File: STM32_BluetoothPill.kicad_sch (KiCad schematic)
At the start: 1 part, among them U1 STM32WBxx

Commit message: Power supply and GPIO
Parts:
- added C? (x2): 4.7u, symbol Device:C_Small
- added C? (x9): 100n, symbol Device:C_Small
- added C? (x2): 12p, symbol Device:C_Small
- added C? (x2): 1u, symbol Device:C_Small
- added C? (x2): 10p, symbol Device:C_Small
- added C?: 10n, symbol Device:C_Small
- added C?: 100p, symbol Device:C_Small
- added D?: GRN, symbol Device:LED_Small
- added D?: PWR, symbol Device:LED_Small
- added D?: RED, symbol Device:LED_Small
- added D?: BLU, symbol Device:LED_Small
- added J?: USB_C_Receptacle_USB2.0, symbol Connector:USB_C_Receptacle_USB2.0
- added J? (x2): Conn_01x20, symbol Connector_Generic:Conn_01x20
- added J?: Conn_01x05, symbol Connector_Generic:Conn_01x05
- added JP?: Jumper_3_Open, symbol Jumper:Jumper_3_Open
- added L?: L_Small, symbol Device:L_Small
- added R?: NC, symbol Device:R_Small
- added R? (x4): 680, symbol Device:R_Small
- added R?: 1k, symbol Device:R_Small
- added R?: 10k, symbol Device:R_Small
- added R? (x2): 5.1k, symbol Device:R_Small
- added R?: 0, symbol Device:R_Small
- added SW?: Reset, symbol Switch:SW_Push
- added SW?: User PB, symbol Switch:SW_Push
- added U?: USBLC6-2SC6, Package_TO_SOT_SMD:SOT-23-6, symbol Power_Protection:USBLC6-2SC6
- added U?: LD3985M33R_SOT23, Package_TO_SOT_SMD:SOT-23-5, symbol Regulator_Linear:LD3985M33R_SOT23
- added Y?: 32k768, symbol Device:Crystal_Small
- added Y?: 8M, symbol Device:Crystal_Small
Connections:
- net VBAT: now reaches U1.1 (VBAT)
- net VBAT: now also J?.20 (Pin_20)
- net PA1: now reaches U1.10 (PA1)
- net PA1: now also J?.16 (Pin_16)
- net PA2: now reaches U1.11 (PA2)
- net PA2: now also J?.15 (Pin_15)
- net PA3: now reaches U1.12 (PA3)
- net PA3: now also J?.14 (Pin_14)
- net PA4: now reaches U1.13 (PA4)
- net PA4: now also J?.13 (Pin_13)
- net PA5: now reaches U1.14 (PA5)
- net PA5: now also J?.12 (Pin_12)
- net PA6: now reaches U1.15 (PA6)
- net PA6: now also J?.11 (Pin_11)
- net PA7: now reaches U1.16 (PA7)
- net PA7: now also J?.10 (Pin_10)
- net PA8: now reaches U1.17 (PA8)
- net PA8: now also J?.9 (Pin_9)
- net PA9: now reaches U1.18 (PA9)
- net PA9: now also J?.8 (Pin_8)
- net PB2: now reaches U1.19 (PB2)
- net PB2: now also J?.7 (Pin_7)
- net at U1.2 (PC14-OSC32_IN): now also C?.1, Y?.2
- net +3V3: now reaches U1.20 (VDD), U1.35 (VDD), U1.48 (VDD)
- net +3V3: now also U1.23 (VDDRF), U1.34 (VDDSMPS), U1.40 (VDDUSB), U1.8 (VDDA), C?.1, C?.1, C?.1, C?.1, C?.1, C?.1, C?.2, C?.2, J?.1 (Pin_1), J?.20 (Pin_20), J?.3 (Pin_3), JP?.1 (A), R?.1, R?.1, R?.1, R?.2
- net GND: now reaches U1.22 (VSSRF)
- net GND: now also U1.32 (VSSSMPS), U1.49 (EXP), C?.1, C?.1, C?.1, C?.2, C?.2, C?.2, C?.2, C?.2, C?.2, C?.2, C?.2, C?.2, C?.2, C?.2, C?.2, C?.2, C?.2, C?.2, C?.2, D?.1 (K), D?.1 (K), D?.1 (K), D?.1 (K), J?.1 (Pin_1), J?.19 (Pin_19), J?.2 (Pin_2), J?.4 (Pin_4), J?.A1 (GND), J?.A12 (GND), J?.B1 (GND), J?.B12 (GND), J?.S1 (SHIELD), JP?.3 (B), R?.1, R?.2, SW?.1, SW?.1, U?.2 (GND), U?.2 (GND)
- net at U1.24 (OSC_OUT): now also C?.1, Y?.2
- net at U1.25 (OSC_IN): now also C?.1, Y?.1
- net PB0: now reaches U1.28 (PB0)
- net PB0: now also J?.6 (Pin_6), R?.1
- net PB1: now reaches U1.29 (PB1)
- net PB1: now also J?.7 (Pin_7), R?.1
- net at U1.3 (PC15-OSC32_OUT): now also C?.1, Y?.1
- net PE4: now reaches U1.30 (PE4)
- net PE4: now also J?.8 (Pin_8), R?.1
- net at U1.31 (VFBSMPS): now also C?.2, L?.2, R?.1
- net at U1.33 (VLXSMPS): now also L?.1
- net PA10: now reaches U1.36 (PA10)
- net PA10: now also J?.9 (Pin_9), R?.1
- net USB_N: now reaches U1.37 (PA11)
- net USB_N: now also J?.10 (Pin_10), U?.6 (I/O1)
- net USB_P: now reaches U1.38 (PA12)
- net USB_P: now also J?.11 (Pin_11), U?.4 (I/O2)
- net SWDIO: now reaches U1.39 (PA13)
- net SWDIO: now also J?.2 (Pin_2)
- net at U1.4 (PH3-BOOT0): now also JP?.2 (C)
- net SWCLK: now reaches U1.41 (PA14)
- net SWCLK: now also J?.3 (Pin_3)
- net PA15: now reaches U1.42 (PA15)
- net PA15: now also J?.12 (Pin_12)
- net PB3: now reaches U1.43 (PB3)
- net PB3: now also J?.13 (Pin_13), J?.5 (Pin_5)
- net PB4: now reaches U1.44 (PB4)
- net PB4: now also J?.14 (Pin_14)
- net PB5: now reaches U1.45 (PB5)
- net PB5: now also J?.15 (Pin_15)
- net PB6: now reaches U1.46 (PB6)
- net PB6: now also J?.16 (Pin_16)
- net PB7: now reaches U1.47 (PB7)
- net PB7: now also J?.17 (Pin_17)
- net PB8: now reaches U1.5 (PB8)
- net PB8: now also J?.19 (Pin_19)
- net PB9: now reaches U1.6 (PB9)
- net PB9: now also J?.18 (Pin_18)
- net RESET: now reaches U1.7 (NRST)
- net RESET: now also C?.1, J?.4 (Pin_4), R?.2, SW?.2
- net PA0: now reaches U1.9 (PA0)
- net PA0: now also J?.17 (Pin_17)
- new net: D?.2 (A), R?.2 (x4)
- new net: J?.A5 (CC1), R?.2
- new net: J?.A6 (D+), J?.B6 (D+), U?.3 (I/O2)
- new net: J?.A7 (D-), J?.B7 (D-), U?.1 (I/O1)
- new net: J?.B5 (CC2), R?.1
- new net: C?.1, C?.1, R?.2, U?.5 (VOUT)
- new net: R?.2, SW?.2
- new net: C?.1, U?.4 (BYP)
- new net +5V: C?.1, C?.1, J?.18 (Pin_18), J?.A4 (VBUS), J?.A9 (VBUS), J?.B4 (VBUS), J?.B9 (VBUS), U?.1 (VIN), U?.3 (INH), U?.5 (VBUS)
- no-connect marks 0 -> 4

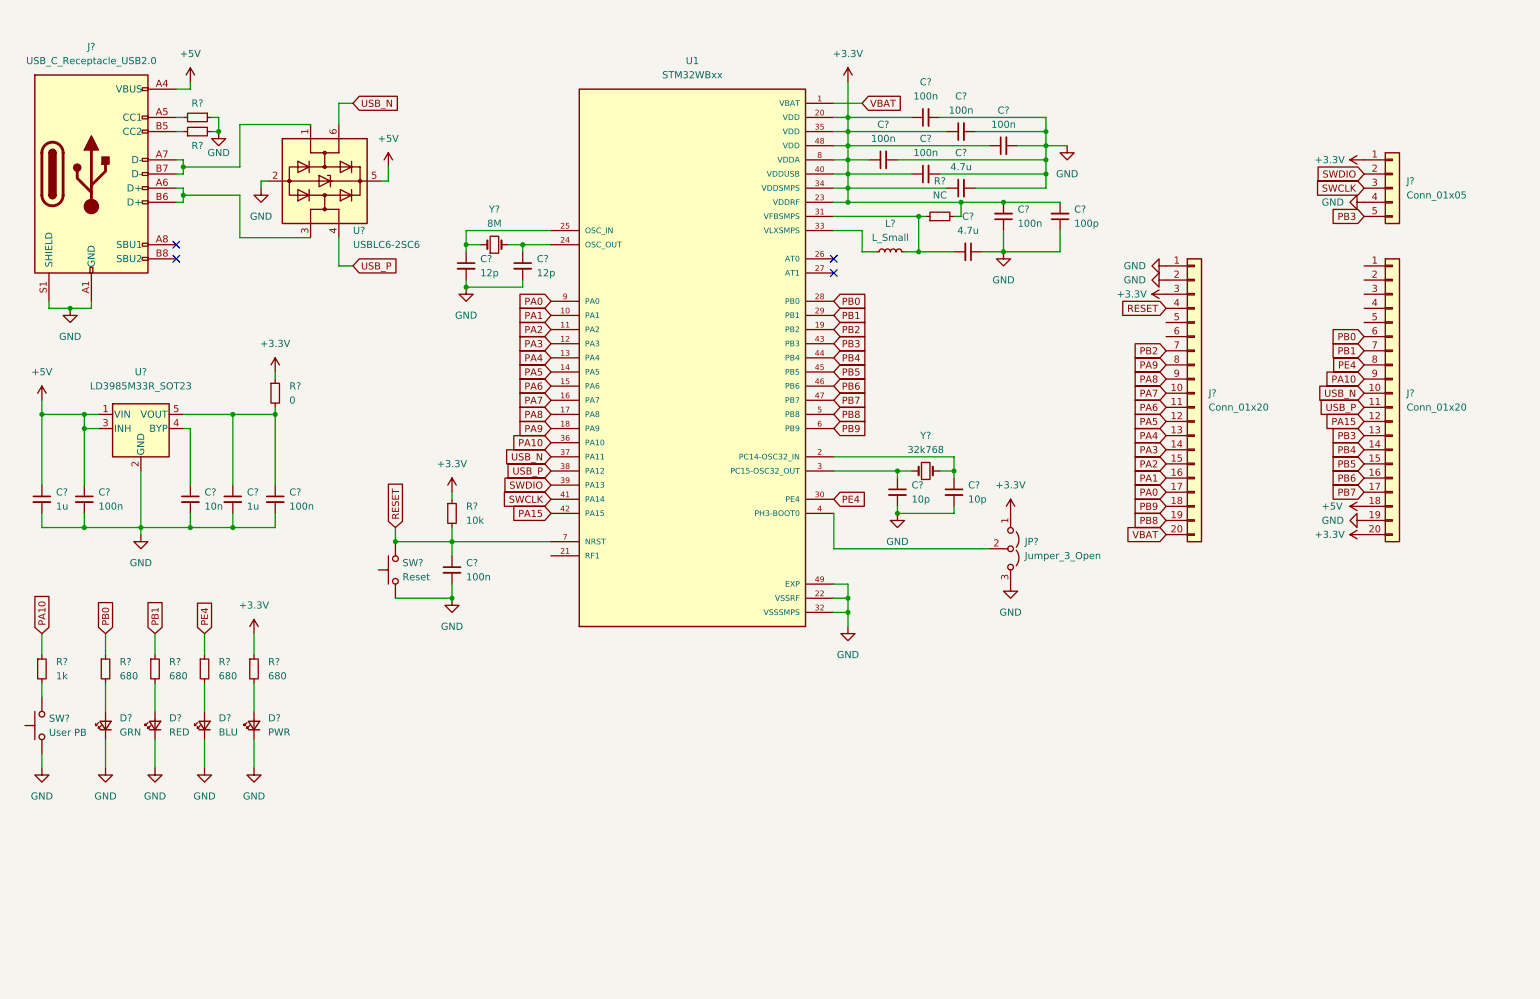
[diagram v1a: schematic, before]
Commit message: RF shield
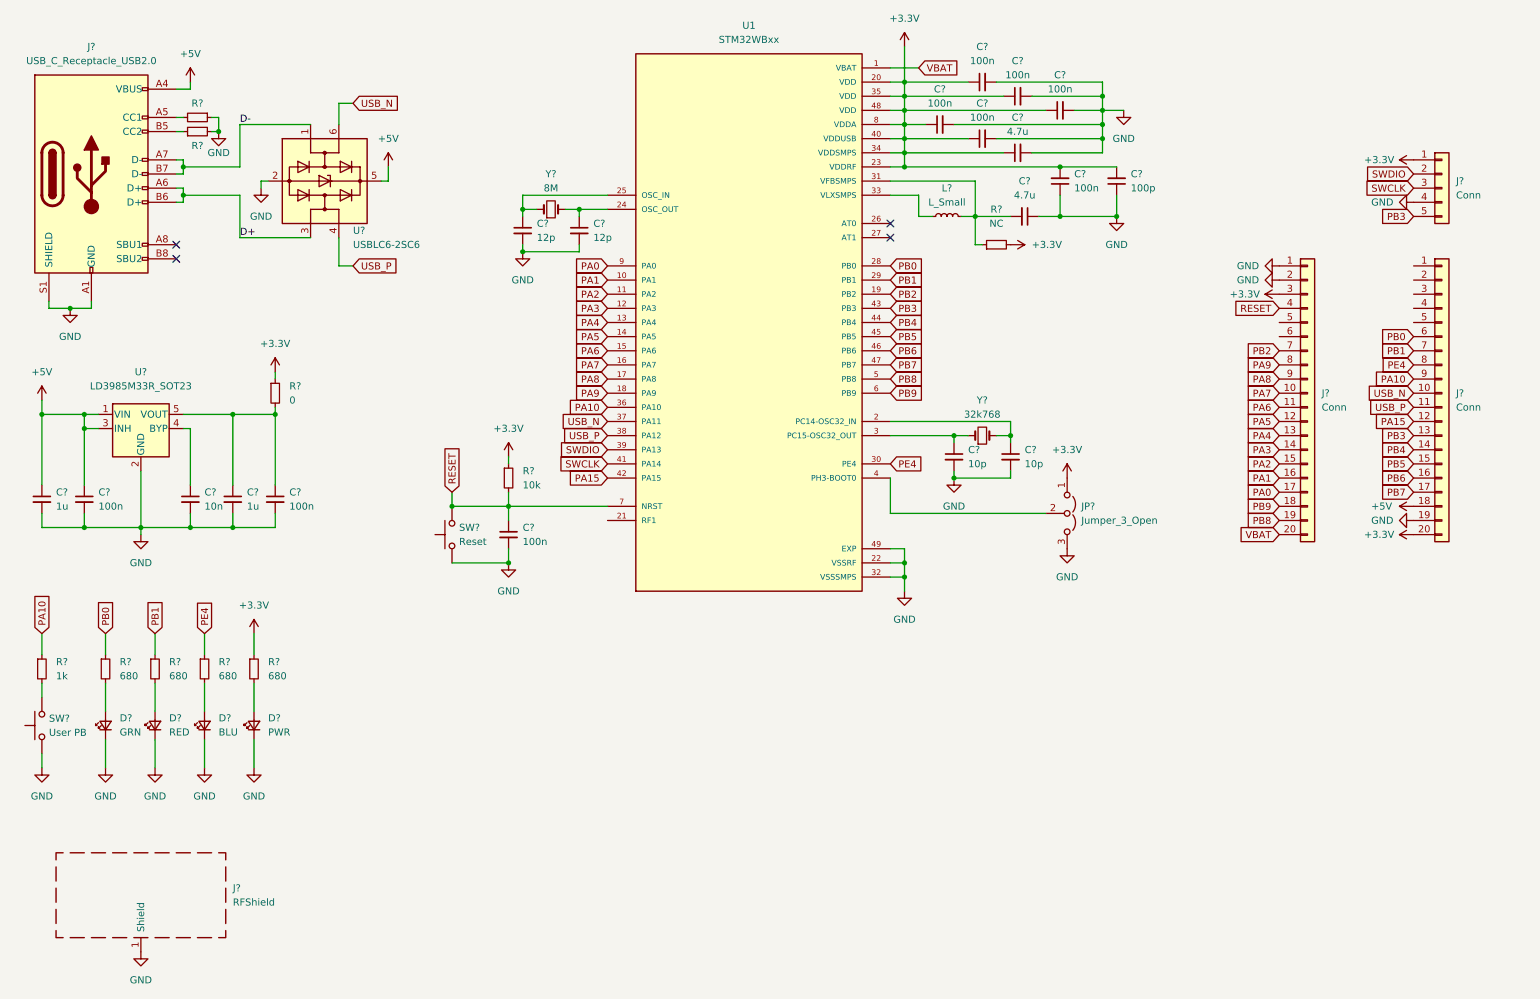
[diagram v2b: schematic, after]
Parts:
- added J?: RFShield, symbol Device:RFShield_OnePiece
- J? (x2): value Conn_01x20 -> Conn
- J?: value Conn_01x05 -> Conn
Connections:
- net GND: now also J?.1 (Shield)
- net D+: now reaches J?.A6 (D+), J?.B6 (D+), U?.3 (I/O2)
- net D-: now reaches J?.A7 (D-), J?.B7 (D-), U?.1 (I/O1)
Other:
- moved on the sheet: C?, J?, JP?, L?, R?, SW?, U1, Y?

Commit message: footprints designated
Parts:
- removed J?: USB_C_Receptacle_USB2.0, symbol Connector:USB_C_Receptacle_USB2.0
- removed J? (x2): Conn, symbol Connector_Generic:Conn_01x20
- removed J?: Conn, symbol Connector_Generic:Conn_01x05
- removed R? (x2): 5.1k, symbol Device:R_Small
- added J1: USB_A, lib:CONN-USB-A-PCB-TRACES, symbol Connector:USB_A
- added J2: Conn, Connector_PinHeader_2.54mm:PinHeader_1x04_P2.54mm_Vertical, symbol Connector_Generic:Conn_01x04
- added J3, J4: Conn, Connector_PinHeader_2.54mm:PinHeader_1x16_P2.54mm_Vertical, symbol Connector_Generic:Conn_01x16
- C1, C10, C11, C12, C13, C14, C15, C16, C17, C18, C19, C2, C3, C4, C5, C6, C7, C8, C9: renamed from C?; footprint (none) -> Capacitor_SMD:C_0603_1608Metric_Pad1.08x0.95mm_HandSolder
- D1, D2, D3, D4: renamed from D?; footprint (none) -> Capacitor_SMD:C_0603_1608Metric_Pad1.08x0.95mm_HandSolder
- J5: renamed from J?; footprint (none) -> RF_Shielding:Laird_Technologies_BMI-S-202-F_16.50x16.50mm
- JP1: renamed from JP?; footprint (none) -> Connector_PinHeader_2.54mm:PinHeader_1x03_P2.54mm_Vertical
- L1: renamed from L?; value L_Small -> 10u; footprint (none) -> Inductor_SMD:L_1206_3216Metric_Pad1.42x1.75mm_HandSolder
- R10, R3, R4, R5, R6, R7, R8, R9: renamed from R?; footprint (none) -> Resistor_SMD:R_0603_1608Metric_Pad0.98x0.95mm_HandSolder
- SW1, SW2: renamed from SW?; footprint (none) -> Button_Switch_SMD:SW_SPST_CK_RS282G05A3
- U1: footprint lib:QFN50P700X700X60-49N -> Package_DFN_QFN:QFN-48-1EP_7x7mm_P0.5mm_EP5.6x5.6mm
- Y1: renamed from Y?; footprint (none) -> Crystal:Crystal_HC49-4H_Vertical
- Y2: renamed from Y?; footprint (none) -> Crystal:Crystal_SMD_SeikoEpson_MC306-4Pin_8.0x3.2mm
- gave numbers to parts that had none: 2
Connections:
- net +3V3: now also J2.1 (Pin_1), J3.2 (Pin_2), J4.16 (Pin_16)
- net +5V: now also J1.1 (VBUS), J4.14 (Pin_14)
- net D+: now also J1.2 (D-)
- net D-: now also J1.3 (D+)
- net GND: now also J1.4 (GND), J2.4 (Pin_4), J3.1 (Pin_1), J4.1 (Pin_1), J4.15 (Pin_15)
- net PA0: now also J3.14 (Pin_14)
- net PA1: now also J3.13 (Pin_13)
- net PA10: now also J4.5 (Pin_5)
- net PA15: now also J4.8 (Pin_8)
- net PA2: now also J3.12 (Pin_12)
- net PA3: now also J3.11 (Pin_11)
- net PA4: now also J3.10 (Pin_10)
- net PA5: now also J3.9 (Pin_9)
- net PA6: now also J3.8 (Pin_8)
- net PA7: now also J3.7 (Pin_7)
- net PA8: now also J3.6 (Pin_6)
- net PA9: now also J3.5 (Pin_5)
- net PB0: now also J4.2 (Pin_2)
- net PB1: now also J4.3 (Pin_3)
- net PB2: now also J3.4 (Pin_4)
- net PB3: now also J4.9 (Pin_9)
- net PB4: now also J4.10 (Pin_10)
- net PB5: now also J4.11 (Pin_11)
- net PB6: now also J4.12 (Pin_12)
- net PB7: now also J4.13 (Pin_13)
- net PB8: now also J3.16 (Pin_16)
- net PB9: now also J3.15 (Pin_15)
- net PE4: now also J4.4 (Pin_4)
- net RESET: now also J3.3 (Pin_3)
- net SWCLK: now also J2.3 (Pin_3)
- net SWDIO: now also J2.2 (Pin_2)
- net USB_N: now also J4.6 (Pin_6)
- net USB_P: now also J4.7 (Pin_7)
- net VBAT: no longer names the net of U1.1 (VBAT)
- no-connect marks 4 -> 3

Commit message: footprints changed gpio names added
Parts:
- C1, C10, C11, C12, C13, C14, C15, C16, C17, C18, C19, C2, C3, C4, C5, C6, C7, C8, C9, D1, D2, D3, D4: footprint Capacitor_SMD:C_0603_1608Metric_Pad1.08x0.95mm_HandSolder -> Capacitor_SMD:C_0603_1608Metric
- R10, R3, R4, R5, R6, R7, R8, R9: footprint Resistor_SMD:R_0603_1608Metric_Pad0.98x0.95mm_HandSolder -> Resistor_SMD:R_0603_1608Metric
- Y1: footprint Crystal:Crystal_HC49-4H_Vertical -> Crystal:Crystal_SMD_HC49-SD
- Y2: footprint Crystal:Crystal_SMD_SeikoEpson_MC306-4Pin_8.0x3.2mm -> Crystal:Crystal_SMD_G8-2Pin_3.2x1.5mm

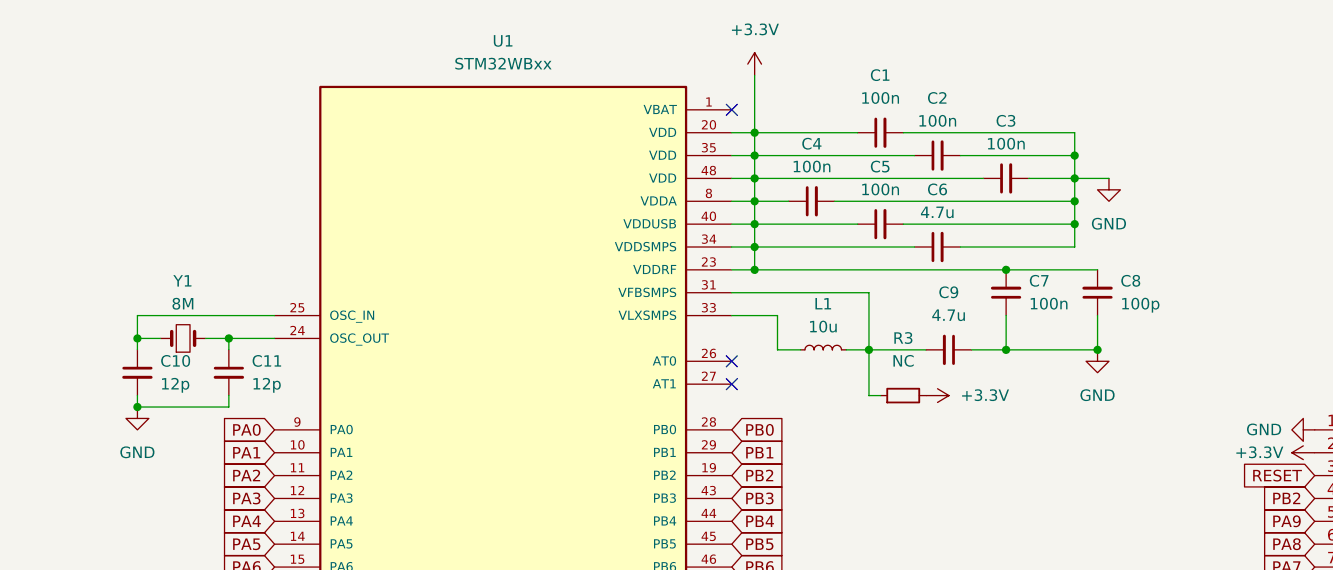
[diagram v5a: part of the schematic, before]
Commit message: move to kicad 6 footprint updates
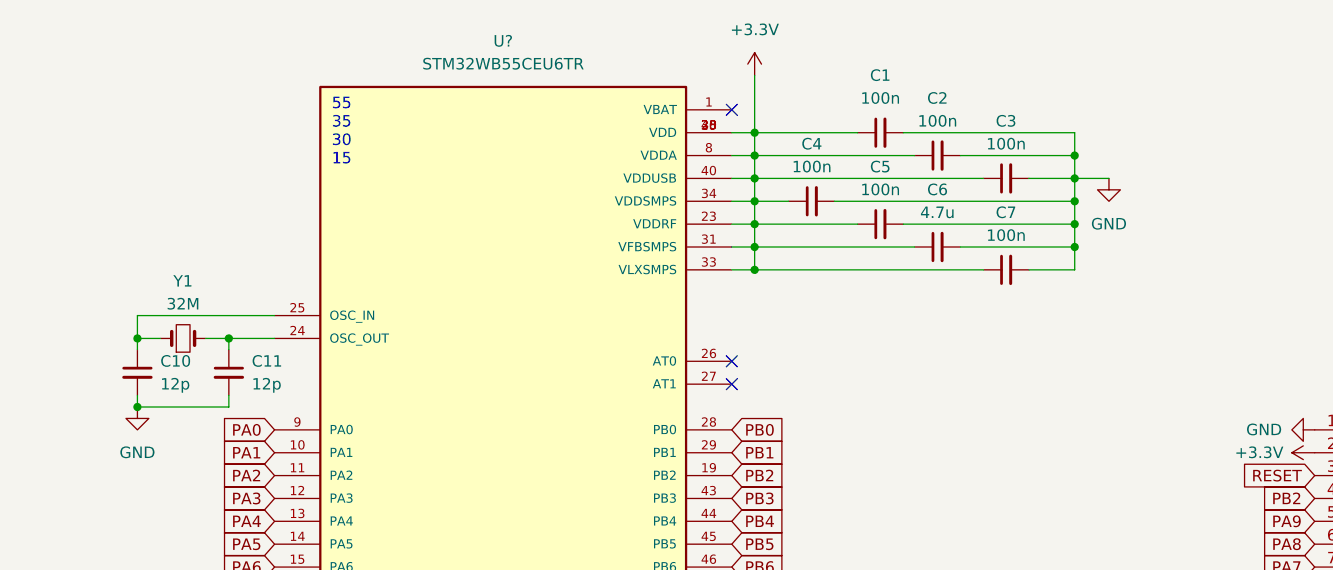
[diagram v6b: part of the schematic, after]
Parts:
- removed C8: 100p, Capacitor_SMD:C_0603_1608Metric, symbol Device:C_Small
- removed C9: 4.7u, Capacitor_SMD:C_0603_1608Metric, symbol Device:C_Small
- removed L1: 10u, Inductor_SMD:L_1206_3216Metric_Pad1.42x1.75mm_HandSolder, symbol Device:L_Small
- removed R3: NC, Resistor_SMD:R_0603_1608Metric, symbol Device:R_Small
- removed U1: STM32WBxx, Package_DFN_QFN:QFN-48-1EP_7x7mm_P0.5mm_EP5.6x5.6mm, symbol STM32WB55CEU6TR:STM32WB55CEU6TR
- added U?: STM32WB55CEU6TR, lib:QFN50P700X700X60-49N, symbol STM32WBxx:STM32WB55CEU6TR
- Y1: value 8M -> 32M; footprint Crystal:Crystal_SMD_HC49-SD -> Crystal:Crystal_HC49-4H_Vertical
- Y2: footprint Crystal:Crystal_SMD_G8-2Pin_3.2x1.5mm -> Crystal:Crystal_SMD_SeikoEpson_MC306-4Pin_8.0x3.2mm
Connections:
- net +3V3: now also C7.1, U?.20 (VDD), U?.23 (VDDRF), U?.31 (VFBSMPS), U?.33 (VLXSMPS), U?.34 (VDDSMPS), U?.35 (VDD), U?.40 (VDDUSB), U?.48 (VDD), U?.8 (VDDA); no longer C7.2
- net GND: now also C7.2, U?.22 (VSSRF), U?.32 (VSSSMPS), U?.49 (EXP); no longer C7.1
- net PA0: now also U?.9 (PA0)
- net PA1: now also U?.10 (PA1)
- net PA10: now also U?.36 (PA10)
- net PA15: now also U?.42 (PA15)
- net PA2: now also U?.11 (PA2)
- net PA3: now also U?.12 (PA3)
- net PA4: now also U?.13 (PA4)
- net PA5: now also U?.14 (PA5)
- net PA6: now also U?.15 (PA6)
- net PA7: now also U?.16 (PA7)
- net PA8: now also U?.17 (PA8)
- net PA9: now also U?.18 (PA9)
- net PB0: now also U?.28 (PB0)
- net PB1: now also U?.29 (PB1)
- net PB2: now also U?.19 (PB2)
- net PB3: now also U?.43 (PB3)
- net PB4: now also U?.44 (PB4)
- net PB5: now also U?.45 (PB5)
- net PB6: now also U?.46 (PB6)
- net PB7: now also U?.47 (PB7)
- net PB8: now also U?.5 (PB8)
- net PB9: now also U?.6 (PB9)
- net PE4: now also U?.30 (PE4)
- net RESET: now also U?.7 (NRST)
- net SWCLK: now also U?.41 (PA14)
- net SWDIO: now also U?.39 (PA13)
- net USB_N: now also U?.37 (PA11)
- net USB_P: now also U?.38 (PA12)
- net at C12.1, Y2.1: now also U?.3 (PC15-OSC32_OUT)
- net at C13.1, Y2.2: now also U?.2 (PC14-OSC32_IN)
- net at JP1.2 (C): now also U?.4 (PH3-BOOT0)
- net at C11.1, Y1.2: now also U?.24 (OSC_OUT)
- net at C10.1, Y1.1: now also U?.25 (OSC_IN)
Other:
- note added: "55 35 30 15"
- moved on the sheet: C7

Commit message: matched low pass filter added
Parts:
- added AE1: Antenna_Shield, RF_Antenna:Texas_SWRA117D_2.4GHz_Right, symbol Device:Antenna_Shield
- added IC1: MLPF-WB-01E3, lib:MLPFWB01E3, symbol MLPF-WB-01E3:MLPF-WB-01E3
- C1, C2, C3, C4, C5, C7: value 100n -> C_Small
- C10: renamed from C12; value 10p -> C_Small
- C11: renamed from C13; value 10p -> C_Small
- C12: renamed from C14; value 1u -> C_Small
- C13: renamed from C15; value 100n -> C_Small
- C14: renamed from C16; value 10n -> C_Small
- C15: renamed from C17; value 1u -> C_Small
- C16: renamed from C18; value 100n -> C_Small
- C17: renamed from C19; value 100n -> C_Small
- C6: value 4.7u -> C_Small
- C8: renamed from C10; value 12p -> C_Small
- C9: renamed from C11; value 12p -> C_Small
- D1: value GRN -> LED_Small
- D2: value RED -> LED_Small
- D3: value BLU -> LED_Small
- D4: value PWR -> LED_Small
- J2: value Conn -> Conn_01x04
- J3, J4: value Conn -> Conn_01x16
- J5: value RFShield -> RFShield_OnePiece
- R1: renamed from R4; value 0 -> R_Small
- R2: renamed from R5; value 10k -> R_Small
- R3: renamed from R6; value 1k -> R_Small
- R4: renamed from R7; value 680 -> R_Small
- R5: renamed from R8; value 680 -> R_Small
- R6: renamed from R9; value 680 -> R_Small
- R7: renamed from R10; value 680 -> R_Small
- SW1: value Reset -> SW_Push
- SW2: value User PB -> SW_Push
- Y1: value 32M -> Crystal_Small
- Y2: value 32k768 -> Crystal_Small
- gave numbers to parts that had none: 1
- renumbered U2 to U1
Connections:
- net GND: now also AE1.2 (Shield), IC1.A2 (GND4), IC1.B1 (GND3), IC1.B2 (GND2), IC1.B3 (GND1)
- net at U2.21 (RF1): now also IC1.A3 (IN)
- net +3V3 renamed +3.3V
- new net: AE1.1 (A), IC1.A1 (OUT)
